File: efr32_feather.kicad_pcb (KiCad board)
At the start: 2 copper layers, 50.8 x 22.9 mm, 32 parts, among them J1 USB, J2 Battery, J3 Feather_1, J4 Feather_2, J5 DEBUG, Q1 DMG2301L, U1 EFR32BG_QFN48, U2 AP2112K-3.3, U3 MCP73831-2-OT, U4 CP2102N-A01-GQFN20, Y1 32768Hz, Y2 38.4MHz

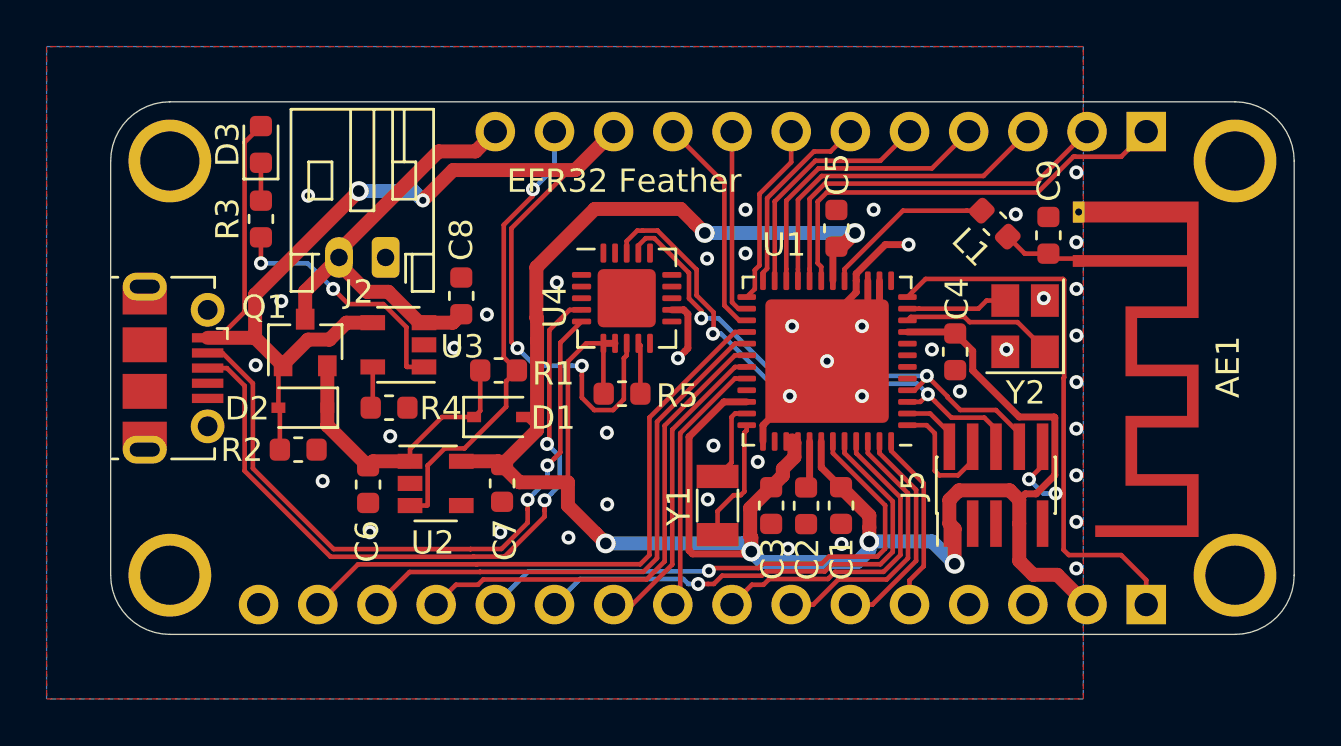
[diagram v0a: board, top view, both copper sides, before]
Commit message: PIN names on silk screen
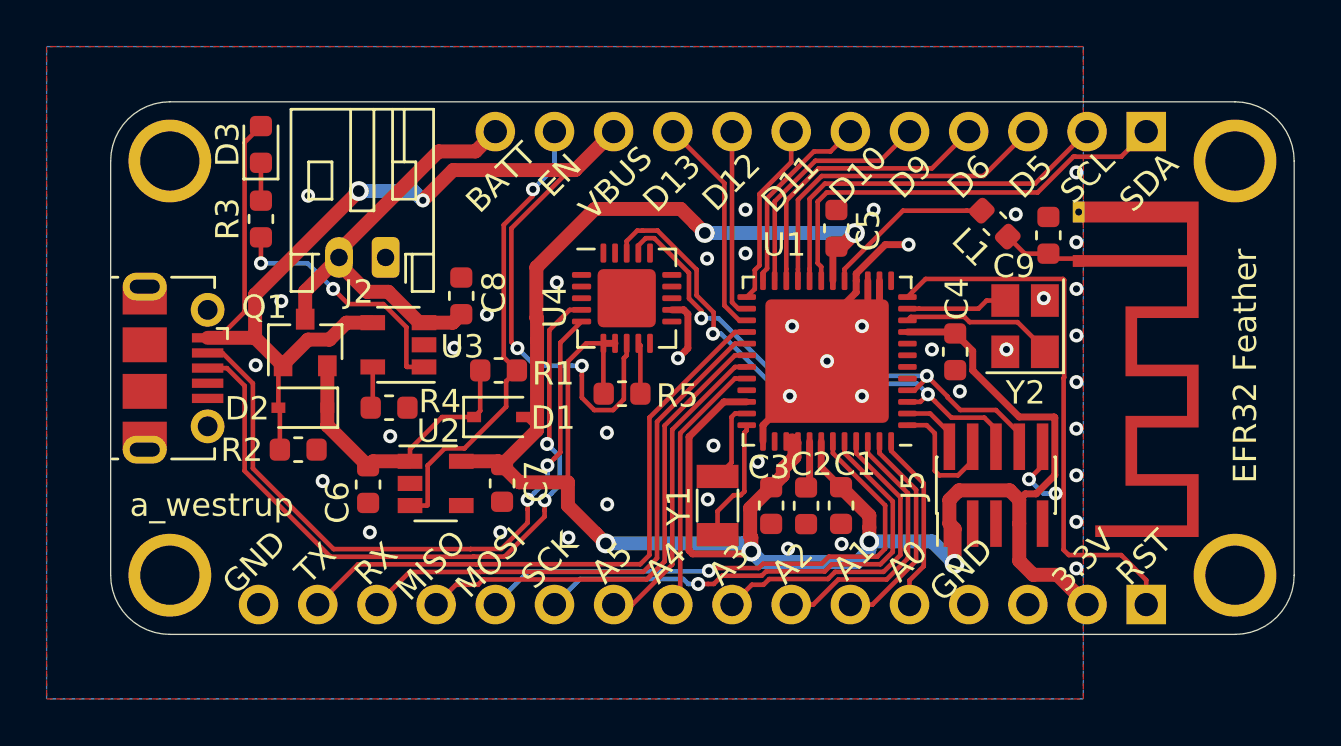
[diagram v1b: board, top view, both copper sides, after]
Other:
- board text added: "3.3V"
- board text added: "A0"
- board text added: "A1"
- board text added: "A2"
- board text added: "A3"
- board text added: "A4"
- board text added: "A5"
- board text added: "BATT"
- board text added: "D10"
- board text added: "D11"
- board text added: "D12"
- board text added: "D13"
- board text added: "D5"
- board text added: "D6"
- board text added: "D9"
- board text added: "EN"
- board text added: "GND"
- board text added: "MISO"
- board text added: "MOSI"
- board text added: "RST"
- board text added: "RX"
- board text added: "SCK"
- board text added: "SCL"
- board text added: "SDA"
- board text added: "TX"
- board text added: "VBUS"
- board text added: "a_westrup"
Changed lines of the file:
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@@
   (general
     (thickness 1.6)
-    (drawings 1)
+    (drawings 29)
     (tracks 533)
     (zones 0)
@@
     (tags "PCB antenna")
     (attr virtual)
-    (fp_text reference AE1 (at 4.55 -6.41 90) (layer F.SilkS)
+    (fp_text reference AE1 (at 4.55 -6.41 90) (layer F.SilkS) hide
       (effects (font (size 1 1) (thickness 0.15)))
     )
@@
     (tags capacitor)
     (attr smd)
-    (fp_text reference C9 (at 2.35 0.03 270) (layer F.SilkS)
+    (fp_text reference C9 (at -1.33 -1.48) (layer F.SilkS)
       (effects (font (size 1 1) (thickness 0.15)))
     )
@@
     (tags resistor)
     (attr smd)
-    (fp_text reference R4 (at -2.22 -0.03) (layer F.SilkS)
+    (fp_text reference R4 (at -2.18 0.27) (layer F.SilkS)
       (effects (font (size 1 1) (thickness 0.15)))
     )
@@
     (tags capacitor)
     (attr smd)
-    (fp_text reference C8 (at 2.41 0 90) (layer F.SilkS)
+    (fp_text reference C8 (at 0.14 1.4 90) (layer F.SilkS)
       (effects (font (size 1 1) (thickness 0.15)))
     )
@@
     (tags SOT-23-5)
     (attr smd)
-    (fp_text reference U2 (at -0.13 2.55) (layer F.SilkS)
+    (fp_text reference U2 (at 0.12 -2.25) (layer F.SilkS)
       (effects (font (size 1 1) (thickness 0.15)))
     )
@@
     (tags capacitor)
     (attr smd)
-    (fp_text reference C7 (at 2.42 -0.13 90) (layer F.SilkS)
+    (fp_text reference C7 (at -0.08 -1.47 90) (layer F.SilkS)
       (effects (font (size 1 1) (thickness 0.15)))
     )
@@
     (tags capacitor)
     (attr smd)
-    (fp_text reference C6 (at 2.44 0.04 90) (layer F.SilkS)
+    (fp_text reference C6 (at 0.77 1.31 90) (layer F.SilkS)
       (effects (font (size 1 1) (thickness 0.15)))
     )
@@
     (tags capacitor)
     (attr smd)
-    (fp_text reference C5 (at 2.31 0.04 270) (layer F.SilkS)
+    (fp_text reference C5 (at -0.08 1.37 270) (layer F.SilkS)
       (effects (font (size 1 1) (thickness 0.15)))
     )
@@
     (tags capacitor)
     (attr smd)
-    (fp_text reference C3 (at -2.28 -1.43 90) (layer F.SilkS)
+    (fp_text reference C3 (at 1.65 -1.6 180) (layer F.SilkS)
       (effects (font (size 1 1) (thickness 0.15)))
     )
@@
     (tags capacitor)
     (attr smd)
-    (fp_text reference C2 (at 2.3 -1.56 90) (layer F.SilkS)
+    (fp_text reference C2 (at -1.77 -1.72 180) (layer F.SilkS)
       (effects (font (size 1 1) (thickness 0.15)))
     )
@@
     (tags capacitor)
     (attr smd)
-    (fp_text reference C1 (at 2.3 -0.03 270) (layer F.SilkS)
+    (fp_text reference C1 (at -1.78 -0.59) (layer F.SilkS)
       (effects (font (size 1 1) (thickness 0.15)))
     )
@@
     )
   )
-  (gr_text "EFR32 Feather" (at 168.79 131.77) (layer F.SilkS)
-    (effects (font (size 1 1) (thickness 0.15)))
-  )
+  (gr_text RST (at 191.11 147.93 45) (layer F.SilkS)
+    (effects (font (size 1 1) (thickness 0.15)))
+  )
+  (gr_text 3.3V (at 188.5 148.04 45) (layer F.SilkS)
+    (effects (font (size 1 1) (thickness 0.15)))
+  )
+  (gr_text GND (at 183.26 148.45 45) (layer F.SilkS)
+    (effects (font (size 1 1) (thickness 0.15)))
+  )
+  (gr_text A0 (at 180.93 148.08 45) (layer F.SilkS)
+    (effects (font (size 1 1) (thickness 0.15)))
+  )
+  (gr_text A1 (at 178.65 148.02 45) (layer F.SilkS)
+    (effects (font (size 1 1) (thickness 0.15)))
+  )
+  (gr_text A2 (at 176.01 148.17 45) (layer F.SilkS)
+    (effects (font (size 1 1) (thickness 0.15)))
+  )
+  (gr_text A3 (at 173.29 148.23 45) (layer F.SilkS)
+    (effects (font (size 1 1) (thickness 0.15)))
+  )
+  (gr_text A4 (at 170.58 148.15 45) (layer F.SilkS)
+    (effects (font (size 1 1) (thickness 0.15)))
+  )
+  (gr_text A5 (at 168.28 148.15 45) (layer F.SilkS)
+    (effects (font (size 1 1) (thickness 0.15)))
+  )
+  (gr_text SCK (at 165.58 148.05 45) (layer F.SilkS)
+    (effects (font (size 1 1) (thickness 0.15)))
+  )
+  (gr_text MOSI (at 163.06 148.15 45) (layer F.SilkS)
+    (effects (font (size 1 1) (thickness 0.15)))
+  )
+  (gr_text MISO (at 160.5 148.27 45) (layer F.SilkS)
+    (effects (font (size 1 1) (thickness 0.15)))
+  )
+  (gr_text RX (at 158.14 148.2 45) (layer F.SilkS)
+    (effects (font (size 1 1) (thickness 0.15)))
+  )
+  (gr_text TX (at 155.54 148.18 45) (layer F.SilkS)
+    (effects (font (size 1 1) (thickness 0.15)))
+  )
+  (gr_text GND (at 152.91 148.15 45) (layer F.SilkS)
+    (effects (font (size 1 1) (thickness 0.15)))
+  )
+  (gr_text SDA (at 191.31 131.82 45) (layer F.SilkS)
+    (effects (font (size 1 1) (thickness 0.15)))
+  )
+  (gr_text SCL (at 188.67 131.56 45) (layer F.SilkS)
+    (effects (font (size 1 1) (thickness 0.15)))
+  )
+  (gr_text D5 (at 186.26 131.58 45) (layer F.SilkS)
+    (effects (font (size 1 1) (thickness 0.15)))
+  )
+  (gr_text D6 (at 183.61 131.59 45) (layer F.SilkS)
+    (effects (font (size 1 1) (thickness 0.15)))
+  )
+  (gr_text D9 (at 181.1 131.58 45) (layer F.SilkS)
+    (effects (font (size 1 1) (thickness 0.15)))
+  )
+  (gr_text D10 (at 178.84 131.51 45) (layer F.SilkS)
+    (effects (font (size 1 1) (thickness 0.15)))
+  )
+  (gr_text D11 (at 175.92 131.88 45) (layer F.SilkS)
+    (effects (font (size 1 1) (thickness 0.15)))
+  )
+  (gr_text D12 (at 173.39 131.81 45) (layer F.SilkS)
+    (effects (font (size 1 1) (thickness 0.15)))
+  )
+  (gr_text D13 (at 170.84 131.86 45) (layer F.SilkS)
+    (effects (font (size 1 1) (thickness 0.15)))
+  )
+  (gr_text VBUS (at 168.43 131.86 45) (layer F.SilkS)
+    (effects (font (size 1 1) (thickness 0.15)))
+  )
+  (gr_text EN (at 166.03 131.53 45) (layer F.SilkS)
+    (effects (font (size 1 1) (thickness 0.15)))
+  )
+  (gr_text BATT (at 163.51 131.62 45) (layer F.SilkS)
+    (effects (font (size 1 1) (thickness 0.15)))
+  )
+  (gr_text a_westrup (at 151.09 145.68) (layer F.SilkS)
+    (effects (font (size 1 1) (thickness 0.15)))
+  )
+  (gr_text "EFR32 Feather" (at 195.45 139.71 90) (layer F.SilkS)
+    (effects (font (size 1 1) (thickness 0.15)))
+  )

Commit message: Reversed pin header, better antenna traces, reset button
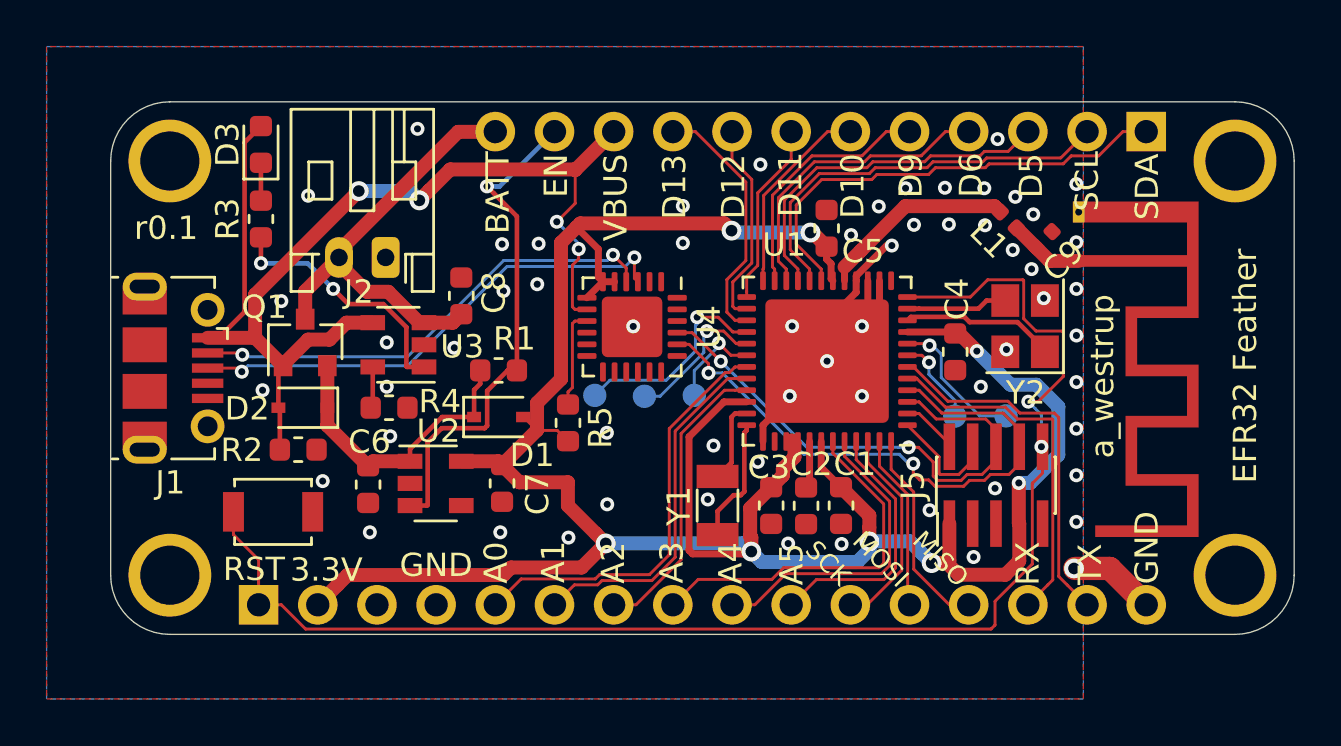
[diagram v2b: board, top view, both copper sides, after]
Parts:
- added SW1: RESET, Button_Switch_SMD:SW_SPST_B3U-1000P, F.Cu at (153.7, 146.0)
- added TP1: PF6, TestPoint:TestPoint_Pad_D1.0mm, B.Cu at (183.0, 141.9)
- added TP2: PF7, TestPoint:TestPoint_Pad_D1.0mm, B.Cu at (185.2, 141.8)
- added TP3: PA5, TestPoint:TestPoint_Pad_D1.0mm, B.Cu at (171.8, 141.0)
- added TP4: PA4, TestPoint:TestPoint_Pad_D1.0mm, B.Cu at (169.7, 141.0)
- added TP5: PA3, TestPoint:TestPoint_Pad_D1.0mm, B.Cu at (167.5, 141.0)
- C9: footprint Capacitor_SMD:C_0603_1608Metric -> Capacitor_SMD:C_0402_1005Metric
- L1: footprint Inductor_SMD:L_0603_1608Metric -> Inductor_SMD:L_0402_1005Metric
- U4: value CP2102N-A01-GQFN20 -> CP2102N-A01-GQFN24; footprint Package_DFN_QFN:QFN-20-1EP_4x4mm_P0.5mm_EP2.5x2.5mm -> Package_DFN_QFN:QFN-24-1EP_4x4mm_P0.5mm_EP2.6x2.6mm
- moved J3 38.1 mm to (153.1, 150.0), turned to 270 degrees
- moved R5 2.64 mm to (166.4, 142.2), turned to 90 degrees
- moved U4 1.25 mm to (169.1, 138.0), turned to 270 degrees
- moved L1 0.60 mm to (185.3, 133.4)
- moved C5 0.42 mm to (177.5, 133.8)
- moved C9 0.26 mm to (186.8, 134.3), turned to 45 degrees
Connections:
- U1 pad 28: /D1_TX -> Net-(TP5-Pad1)
- U1 pad 29: /D0_RX -> Net-(TP4-Pad1)
- U1 pad 30: /D22_MISO -> Net-(TP3-Pad1)
- U1 pad 31: /D19_A5 -> /D14_A0
- U1 pad 32: /D18_A4 -> /D15_A1
- U1 pad 33: Net-(U1-Pad33) -> /D16_A2
- U1 pad 43: /D23_MOSI -> /D17_A3
- U1 pad 44: /D24_SCK -> /D18_A4
- U1 pad 45: /D17_A3 -> /D19_A5
- U1 pad 46: /D16_A2 -> /D24_SCK
- U1 pad 47: /D15_A1 -> /D23_MOSI
- U1 pad 48: /D14_A0 -> /D22_MISO
- U1 pad 5: Net-(U1-Pad5) -> /D0_RX
- U1 pad 6: Net-(U1-Pad6) -> /D1_TX
- U4 pad 12: GND -> Net-(U4-Pad12)
- U4 pad 17: /USB_RX -> Net-(U4-Pad17)
- U4 pad 18: /USB_TX -> Net-(U4-Pad18)
- U4 pad 2: Net-(U4-Pad2) -> GND
- U4 pad 20: Net-(U4-Pad20) -> /USB_RX
- U4 pad 21: (no net) -> /USB_TX
- U4 pad 3: GND -> /USB_D+
- U4 pad 4: /USB_D+ -> /USB_D-
- U4 pad 5: /USB_D- -> +3V3
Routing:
- net /NRESET: track 27.2 -> 60.0 mm
- net /D23_MOSI: track 23.3 -> 7.54 mm, vias 1 -> 0
- net VBUS: track 63.3 -> 50.3 mm
- net /D22_MISO: track 21.2 -> 8.88 mm
- net /D24_SCK: track 21.2 -> 8.95 mm, vias 1 -> 0
- net /D1_TX: track 26.7 -> 15.9 mm
- net /D14_A0: track 7.83 -> 18.2 mm
- net /USB_D+: track 30.9 -> 21.5 mm
- net Net-(TP5-Pad1): track 0.00 -> 8.98 mm, vias 0 -> 1
- net /USB_D-: track 29.4 -> 20.7 mm
- net /D0_RX: track 23.9 -> 15.4 mm
- net Net-(TP4-Pad1): track 0.00 -> 6.23 mm, vias 0 -> 1
- net Net-(TP2-Pad1): track 0.00 -> 6.10 mm, vias 0 -> 1
- net /D15_A1: track 9.38 -> 15.4 mm
- net Net-(TP3-Pad1): track 0.00 -> 4.09 mm, vias 0 -> 1
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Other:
- board text added: "r0.1"

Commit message: r0.2: moved antenna matching components, more silk screen
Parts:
- moved L1 5.60 mm to (179.7, 133.9), turned to 225 degrees
- moved C9 5.22 mm to (181.7, 133.4), turned to 270 degrees
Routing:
- net Net-(AE1-Pad1): track 3.26 -> 9.48 mm
- net Net-(L1-Pad2): track 8.46 -> 2.25 mm
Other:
- board text added: "+"
- board text added: "-"
- board text added: "."
- board text added: "CK"
- board text added: "CLK"
- board text added: "IO"
- board text added: "MI"
- board text added: "MO"
- board text added: "r0.2"
- board text removed: "MISO"
- board text removed: "MOSI"
- board text removed: "SCK"
- board text removed: "r0.1"

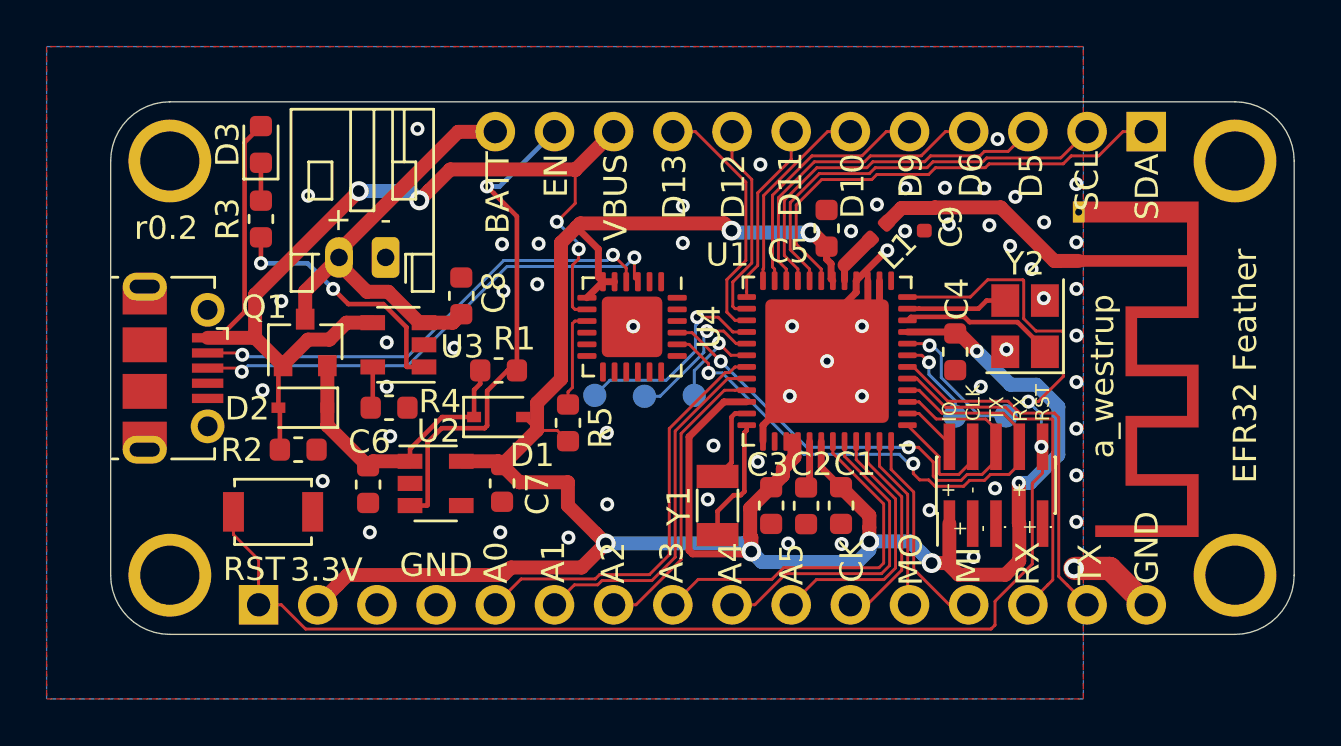
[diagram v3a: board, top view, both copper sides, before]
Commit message: Add ESD protection for USB
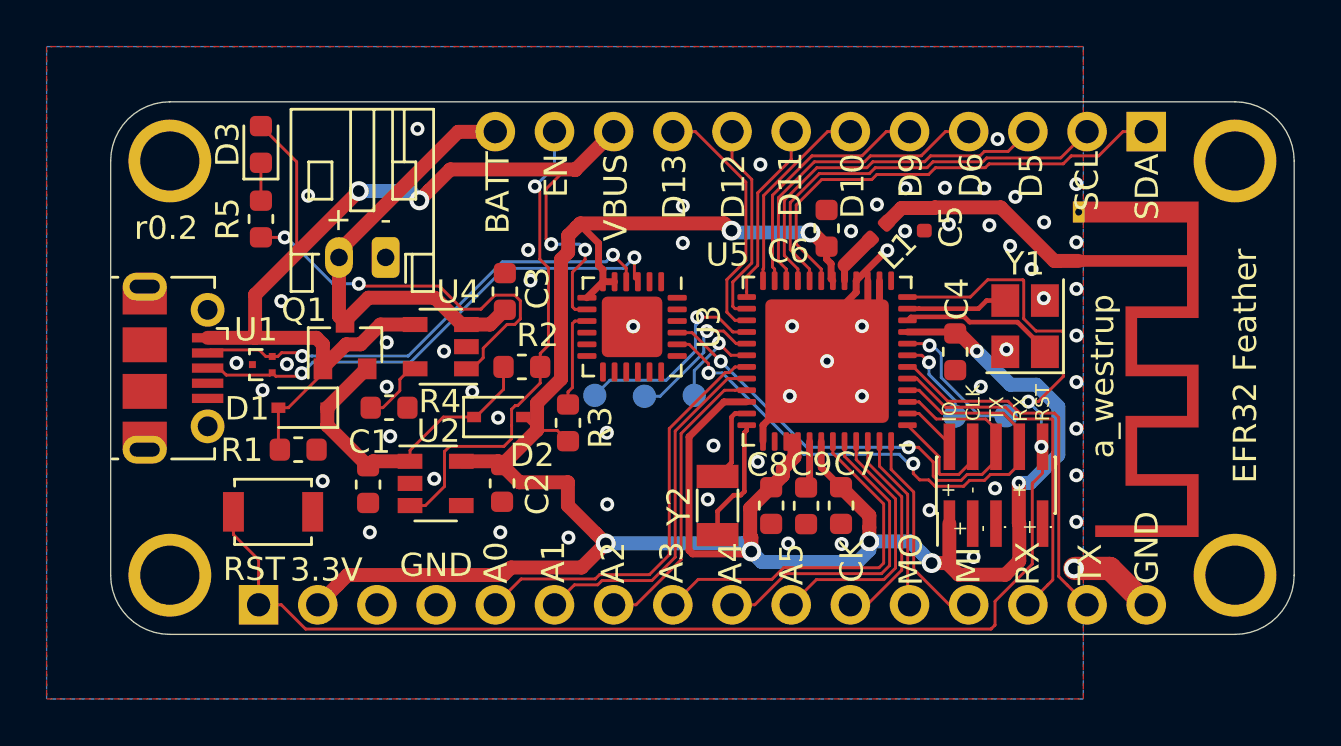
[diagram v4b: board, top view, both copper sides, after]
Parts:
- added U1: TPD2EUSB30, Package_TO_SOT_SMD:Texas_DRT-3, F.Cu at (153.3, 139.7)
- moved C3 1.88 mm to (163.7, 136.5)
- moved U4 1.82 mm to (160.9, 138.9)
- moved Q1 1.71 mm to (156.8, 138.8)
- moved R2 1.01 mm to (164.4, 139.8)
- renumbered C6 to C1, C7 to C2, C8 to C3, C9 to C5, C5 to C6, C1 to C7, C3 to C8, C2 to C9, D2 to D1, D1 to D2, J3 to J1, J1 to J2, J2 to J3, R2 to R1, R1 to R2, R5 to R3, R3 to R5, U4 to U3, U3 to U4, U1 to U5, Y2 to Y1, Y1 to Y2
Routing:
- net Net-(R5-Pad1): track 10.9 -> 17.0 mm
- net Net-(C1-Pad1): track 12.9 -> 14.1 mm
- net Net-(R4-Pad2): track 1.79 -> 2.89 mm
- net +BATT: track 19.1 -> 20.1 mm
- net /EN: track 21.7 -> 20.9 mm
- net VBUS: track 50.3 -> 50.9 mm
- net GND: vias 61 -> 64
